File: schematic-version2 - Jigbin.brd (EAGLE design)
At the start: 47 x 28 mm, 56 parts, among them J2 FTDI_DEVICE, M1 WIRELESS-NRF24L01, Q1 8MHz, T1 NMOS, T2 NMOS, T3 NMOS, T4 NMOS, U1 ATMEGA328P_TQFP, U2 GY-521MPU6050

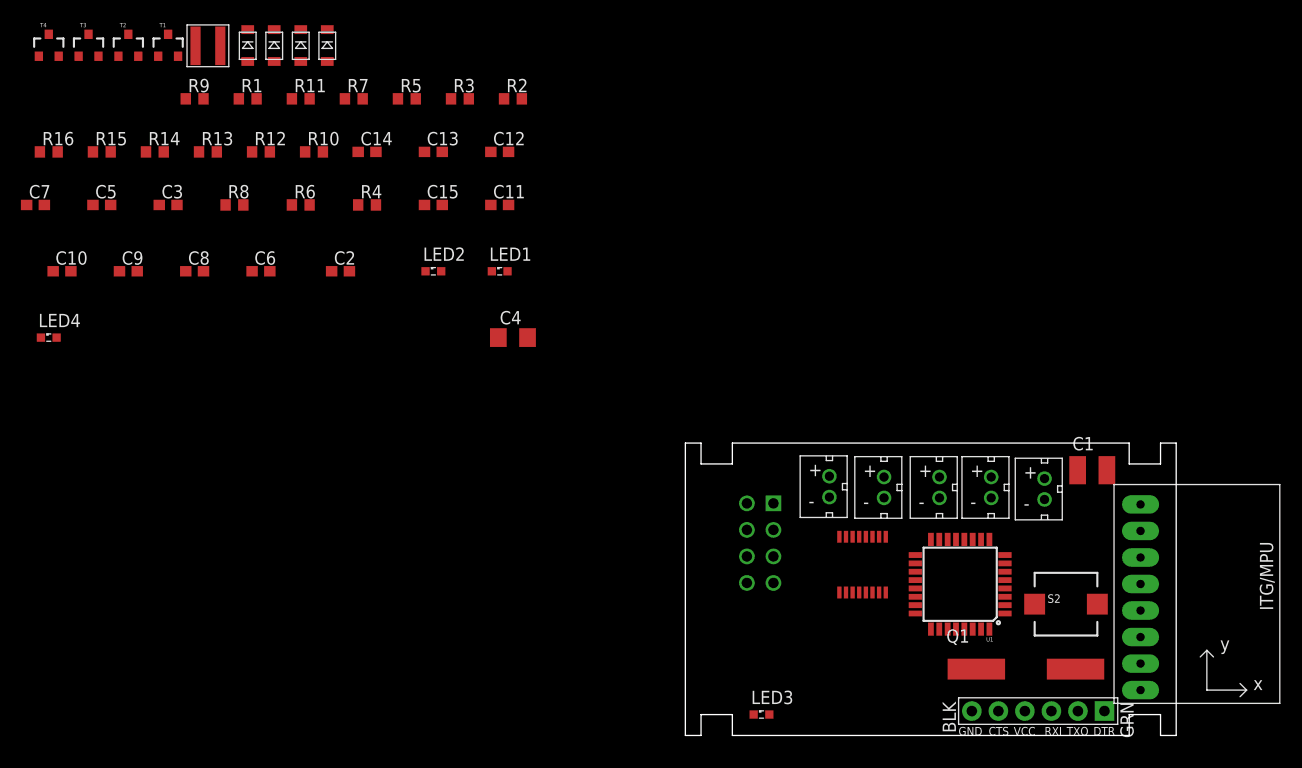
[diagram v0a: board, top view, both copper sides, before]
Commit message: Added anohter finished version
Need to fix clearence issues
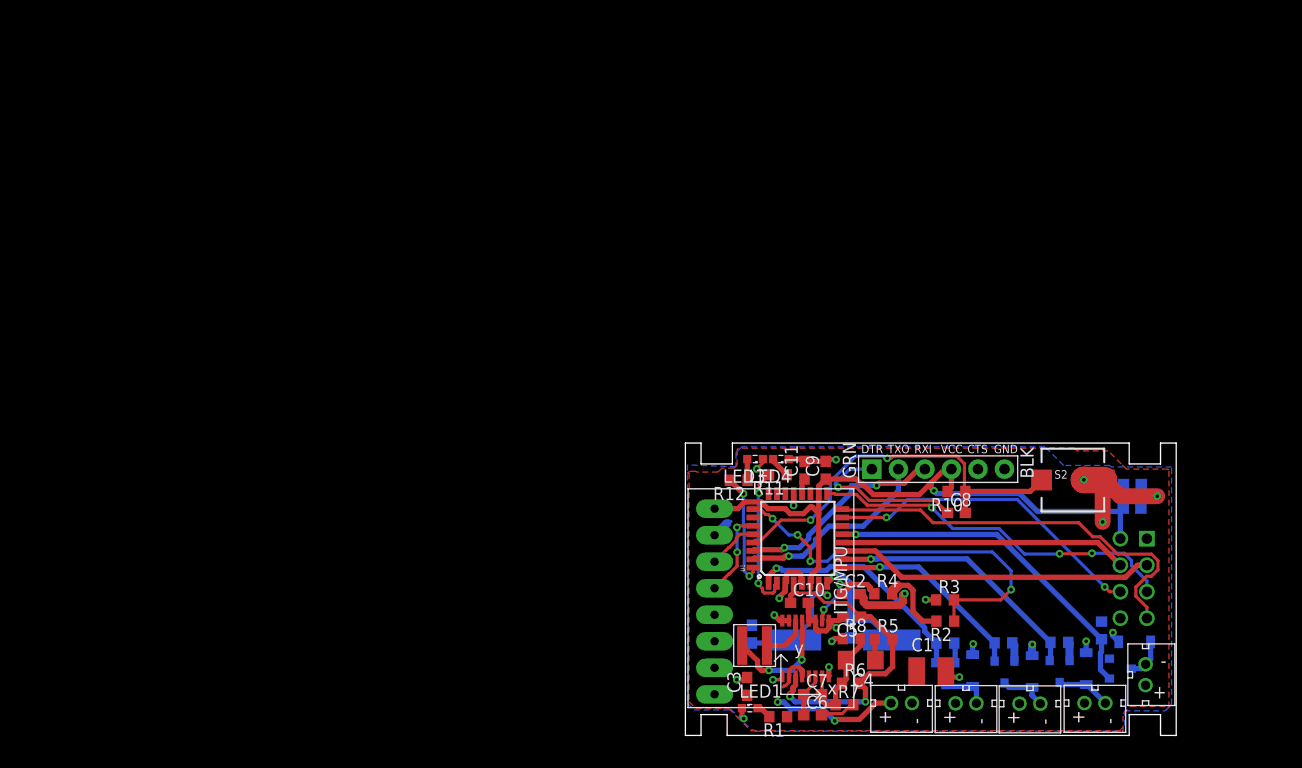
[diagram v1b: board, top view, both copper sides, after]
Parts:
- removed LED2: RED, led:SML0603
- removed R9: 820, rcl:R0603
- moved T4 118.6 mm to (41.6, 6.40), flipped to the bottom, turned to 90 degrees
- moved R16 110.7 mm to (39.9, 10.1), flipped to the bottom, turned to 270 degrees
- moved T3 110.6 mm to (35.8, 6.17), flipped to the bottom, turned to 180 degrees
- moved T2 103.1 mm to (30.6, 6.12), flipped to the bottom, turned to 180 degrees
- moved R15 103.0 mm to (35.8, 8.92), flipped to the bottom
- moved D4 102.4 mm to (43.1, 8.97), flipped to the bottom, turned to 270 degrees
- moved D3 98.0 mm to (38.4, 6.38), flipped to the bottom
- moved T1 95.6 mm to (24.9, 5.97), flipped to the bottom, turned to 180 degrees
- moved R14 93.9 mm to (30.5, 8.86), flipped to the bottom
- moved D2 92.2 mm to (33.2, 6.10), flipped to the bottom
- moved C7 87.9 mm to (12.2, 3.96)
- moved D1 86.0 mm to (27.5, 6.20), flipped to the bottom
- moved R13 84.8 mm to (24.9, 8.84), flipped to the bottom
- moved C5 81.9 mm to (15.9, 11.4), turned to 180 degrees
- moved C14 80.8 mm to (42.8, 21.7), flipped to the bottom, turned to 180 degrees
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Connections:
- removed net N$11: LED2.A, R9.1
- net GND: no longer LED2.C
- net V_REG_OUT: no longer R9.2
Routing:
- net V_REG_OUT: track 0.00 -> 95.1 mm, vias 0 -> 3
- net GND: track 0.00 -> 57.6 mm, vias 0 -> 17
- net N$2: track 0.00 -> 39.7 mm, vias 0 -> 2
- net MISO: track 0.00 -> 39.3 mm
- net V_BAT: track 0.00 -> 38.4 mm, vias 0 -> 4
- net SCK: track 0.00 -> 35.5 mm, vias 0 -> 3
- net PWM4: track 0.00 -> 33.1 mm, vias 0 -> 1
- net MOSI: track 0.00 -> 31.0 mm, vias 0 -> 2
- net CE: track 0.00 -> 30.7 mm
- net PWR: track 0.00 -> 29.9 mm, vias 0 -> 6
- net CSN: track 0.00 -> 27.5 mm
- net PWM3: track 0.00 -> 25.0 mm, vias 0 -> 1
- net PWM1: track 0.00 -> 22.5 mm, vias 0 -> 1
- net RXD: track 0.00 -> 20.3 mm, vias 0 -> 2
- net PWM2: track 0.00 -> 19.3 mm, vias 0 -> 1
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- added copper zone on layer 16, net GND
- added copper zone on layer 1, net PWR
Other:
- outline, holes or cut-outs redrawn

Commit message: Fixed problems in my version 2
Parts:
- moved C8 0.86 mm to (26.0, 20.4)
- moved R10 0.81 mm to (26.0, 22.6)
- moved J2 0.56 mm to (24.2, 24.9)
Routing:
- net GND: track 57.6 -> 61.7 mm
- net RXD: track 20.3 -> 22.9 mm, vias 2 -> 3
- net N$4: track 11.1 -> 13.2 mm
- net PWM2: track 19.3 -> 21.2 mm, vias 1 -> 3
- net PWM3: track 25.0 -> 26.4 mm, vias 1 -> 3
- net MOSI: track 31.0 -> 32.0 mm
- net PWR: track 29.9 -> 30.7 mm
- net N$2: track 39.7 -> 40.5 mm
- net N$16: track 9.45 -> 10.2 mm
- net TXD: track 19.0 -> 18.4 mm
- net PWM4: vias 1 -> 3

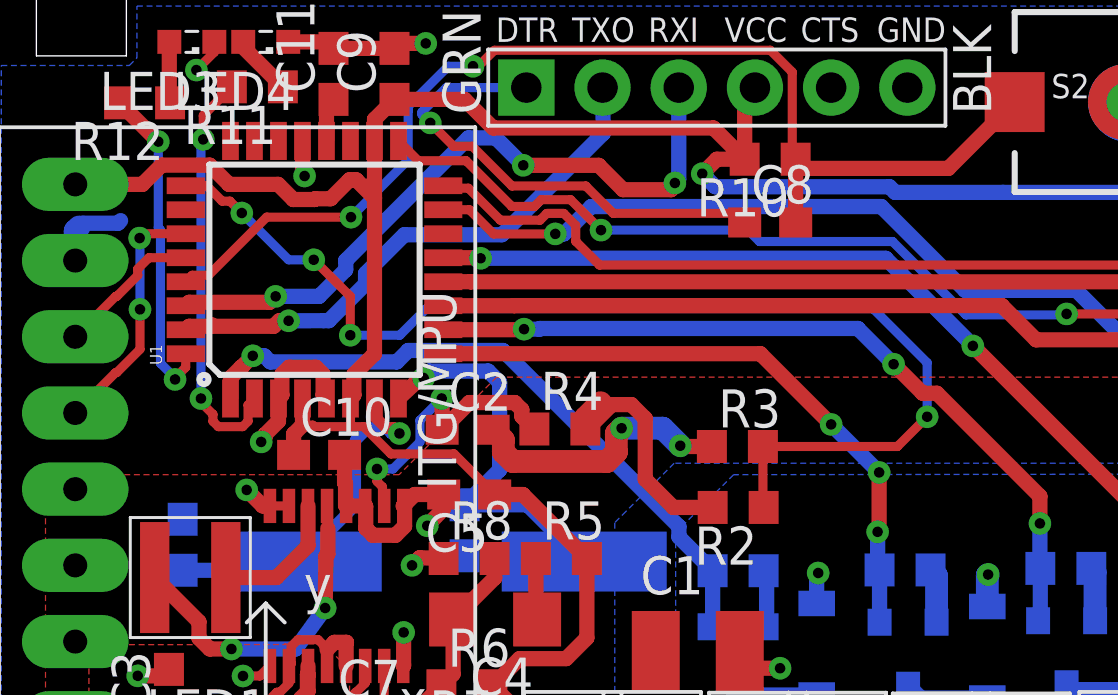
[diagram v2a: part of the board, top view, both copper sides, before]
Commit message: Changed V_BAT trace from thin to thic
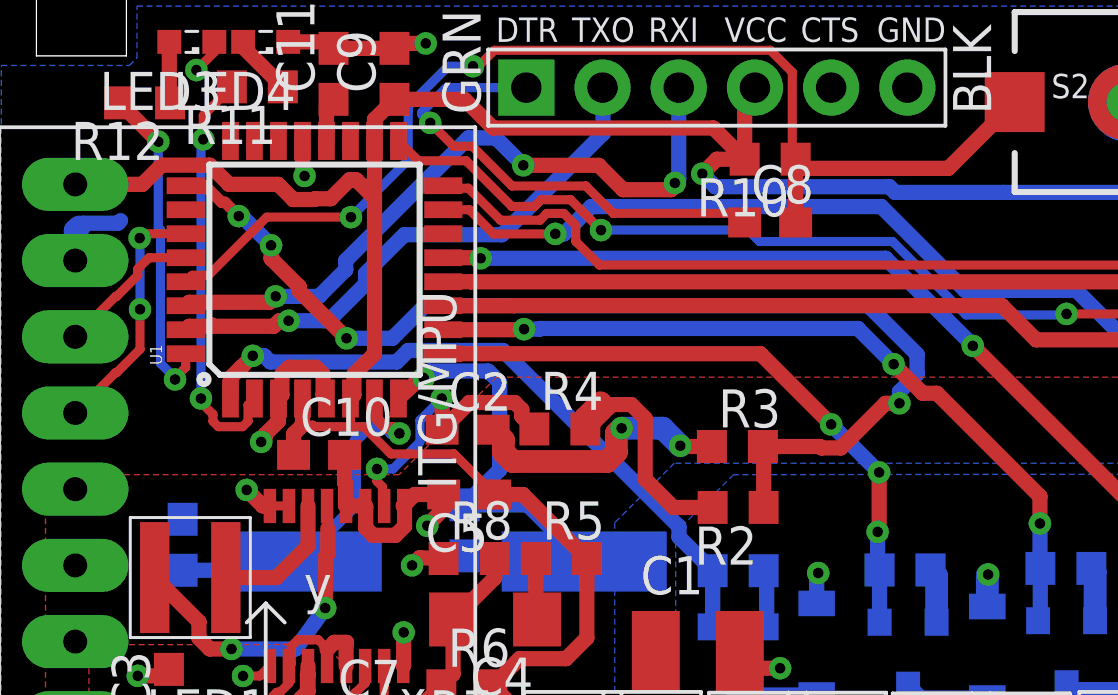
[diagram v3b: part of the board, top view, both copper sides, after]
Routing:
- net V_BAT: track 38.4 -> 37.1 mm
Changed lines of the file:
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@@
 <contactref element="R3" pad="2"/>
 <contactref element="U1" pad="25"/>
-<via x="8.34636875" y="20.76203125" extent="1-16" drill="0.35"/>
-<wire x1="6.477" y1="21.6722" x2="7.17586875" y2="21.6722" width="0.3048" layer="1"/>
-<wire x1="7.17586875" y1="21.6722" x2="7.68986875" y2="21.1582" width="0.3048" layer="1"/>
-<wire x1="7.68986875" y1="21.1582" x2="7.9502" y2="21.1582" width="0.3048" layer="1"/>
-<wire x1="7.9502" y1="21.1582" x2="8.34636875" y2="20.76203125" width="0.3048" layer="1"/>
-<wire x1="8.34636875" y1="20.76203125" x2="9.906" y2="19.2024" width="0.3048" layer="16"/>
-<wire x1="9.906" y1="19.2024" x2="10.7442" y2="19.2024" width="0.3048" layer="16"/>
-<via x="10.7442" y="19.2024" extent="1-16" drill="0.35"/>
-<wire x1="10.7442" y1="19.2024" x2="11.9634" y2="17.9832" width="0.3048" layer="1"/>
-<wire x1="11.9634" y1="17.9832" x2="11.9634" y2="16.6878" width="0.3048" layer="1"/>
-<via x="11.9634" y="16.6878" extent="1-16" drill="0.35"/>
-<wire x1="11.9634" y1="16.6878" x2="13.61153125" y2="16.6878" width="0.3048" layer="16"/>
-<wire x1="14.49773125" y1="17.574" x2="13.61153125" y2="16.6878" width="0.3048" layer="16"/>
-<wire x1="25.7166" y1="12.9794" x2="25.7166" y2="10.9728" width="0.3048" layer="1"/>
 <wire x1="25.7166" y1="10.9728" x2="25.742" y2="10.9474" width="0.3048" layer="1"/>
-<wire x1="25.7166" y1="12.9794" x2="30.2006" y2="12.9794" width="0.3048" layer="1"/>
-<wire x1="30.2006" y1="12.9794" x2="31.1912" y2="13.97" width="0.3048" layer="1"/>
-<via x="31.1912" y="13.97" extent="1-16" drill="0.35"/>
-<wire x1="31.1912" y1="13.97" x2="31.1912" y2="15.7734" width="0.3048" layer="16"/>
-<wire x1="31.1912" y1="15.7734" x2="29.3906" y2="17.574" width="0.3048" layer="16"/>
-<wire x1="29.3906" y1="17.574" x2="14.49773125" y2="17.574" width="0.3048" layer="16"/>
+<wire x1="25.742" y1="10.9474" x2="25.742" y2="12.954" width="0.508" layer="1"/>
+<wire x1="25.742" y1="12.954" x2="25.7166" y2="12.9794" width="0.508" layer="1"/>
+<via x="30.268103125" y="14.418503125" extent="1-16" drill="0.35"/>
+<wire x1="27.66580625" y1="12.9314" x2="28.31579375" y2="12.9314" width="0.508" layer="1"/>
+<wire x1="29.802896875" y1="14.418503125" x2="30.268103125" y2="14.418503125" width="0.508" layer="1"/>
+<wire x1="28.31579375" y1="12.9314" x2="29.802896875" y2="14.418503125" width="0.508" layer="1"/>
+<wire x1="25.7166" y1="12.9794" x2="27.61780625" y2="12.9794" width="0.508" layer="1"/>
+<wire x1="27.61780625" y1="12.9794" x2="27.66580625" y2="12.9314" width="0.508" layer="1"/>
+<via x="11.8364" y="16.5862" extent="1-16" drill="0.35"/>
+<wire x1="30.8582" y1="15.39760625" x2="30.8582" y2="16.04759375" width="0.508" layer="16"/>
+<wire x1="13.36625" y1="16.5862" x2="11.8364" y2="16.5862" width="0.508" layer="16"/>
+<wire x1="30.268103125" y1="14.418503125" x2="30.268103125" y2="14.807509375" width="0.508" layer="16"/>
+<wire x1="30.268103125" y1="14.807509375" x2="30.8582" y2="15.39760625" width="0.508" layer="16"/>
+<wire x1="14.45565" y1="17.6756" x2="13.36625" y2="16.5862" width="0.508" layer="16"/>
+<wire x1="30.8582" y1="16.04759375" x2="29.23019375" y2="17.6756" width="0.508" layer="16"/>
+<wire x1="29.23019375" y1="17.6756" x2="14.45565" y2="17.6756" width="0.508" layer="16"/>
+<via x="9.3218" y="19.685" extent="1-16" drill="0.35"/>
+<wire x1="11.8364" y1="16.5862" x2="10.2588" y2="18.1638" width="0.508" layer="1"/>
+<wire x1="10.2588" y1="18.1638" x2="10.2588" y2="18.30819375" width="0.508" layer="1"/>
+<wire x1="9.3218" y1="19.24519375" x2="9.3218" y2="19.685" width="0.508" layer="1"/>
+<wire x1="10.2588" y1="18.30819375" x2="9.3218" y2="19.24519375" width="0.508" layer="1"/>
+<wire x1="9.3218" y1="19.685" x2="8.34636875" y2="20.66043125" width="0.508" layer="16"/>
+<wire x1="8.34636875" y1="20.66043125" x2="8.24476875" y2="20.66043125" width="0.508" layer="16"/>
+<via x="8.24476875" y="20.66043125" extent="1-16" drill="0.35"/>
+<wire x1="8.24476875" y1="20.66043125" x2="7.7851" y2="21.1201" width="0.381" layer="1"/>
+<wire x1="7.7851" y1="21.1201" x2="7.6740875" y2="21.1201" width="0.381" layer="1"/>
+<wire x1="7.6740875" y1="21.1201" x2="7.1219875" y2="21.6722" width="0.381" layer="1"/>
+<wire x1="7.1219875" y1="21.6722" x2="6.477" y2="21.6722" width="0.381" layer="1"/>
 </signal>
 <signal name="DTR">
